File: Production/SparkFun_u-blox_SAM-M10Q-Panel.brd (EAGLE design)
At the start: 184.2 x 137.2 mm, 906 parts, among them J1 Qwiic Right Angle, J10 Qwiic Right Angle, J11 BOOT, J13 Qwiic Right Angle, J14 Qwiic Right Angle, J15 BOOT, J17 Qwiic Right Angle, J18 Qwiic Right Angle, J19 BOOT, J2 Qwiic Right Angle, J21 Qwiic Right Angle, J22 Qwiic Right Angle, J23 BOOT, J25 Qwiic Right Angle, J26 Qwiic Right Angle, J27 BOOT, J29 Qwiic Right Angle, J30 Qwiic Right Angle, J31 BOOT, J33 Qwiic Right Angle, J34 Qwiic Right Angle, J35 BOOT, J37 Qwiic Right Angle, J38 Qwiic Right Angle, J39 BOOT, J4 BOOT, J41 Qwiic Right Angle, J42 Qwiic Right Angle, J43 BOOT, J45 Qwiic Right Angle, J46 Qwiic Right Angle, J47 BOOT, J5 Qwiic Right Angle, J6 Qwiic Right Angle, J7 BOOT, J9 Qwiic Right Angle, U1 U-BLOX_SAM_M10Q-00B, U10 U-BLOX_SAM_M10Q-00B, U11 U-BLOX_SAM_M10Q-00B, U12 U-BLOX_SAM_M10Q-00B, U2 U-BLOX_SAM_M10Q-00B, U3 U-BLOX_SAM_M10Q-00B, U4 U-BLOX_SAM_M10Q-00B, U5 U-BLOX_SAM_M10Q-00B, U6 U-BLOX_SAM_M10Q-00B, U7 U-BLOX_SAM_M10Q-00B, U8 U-BLOX_SAM_M10Q-00B, U9 U-BLOX_SAM_M10Q-00B

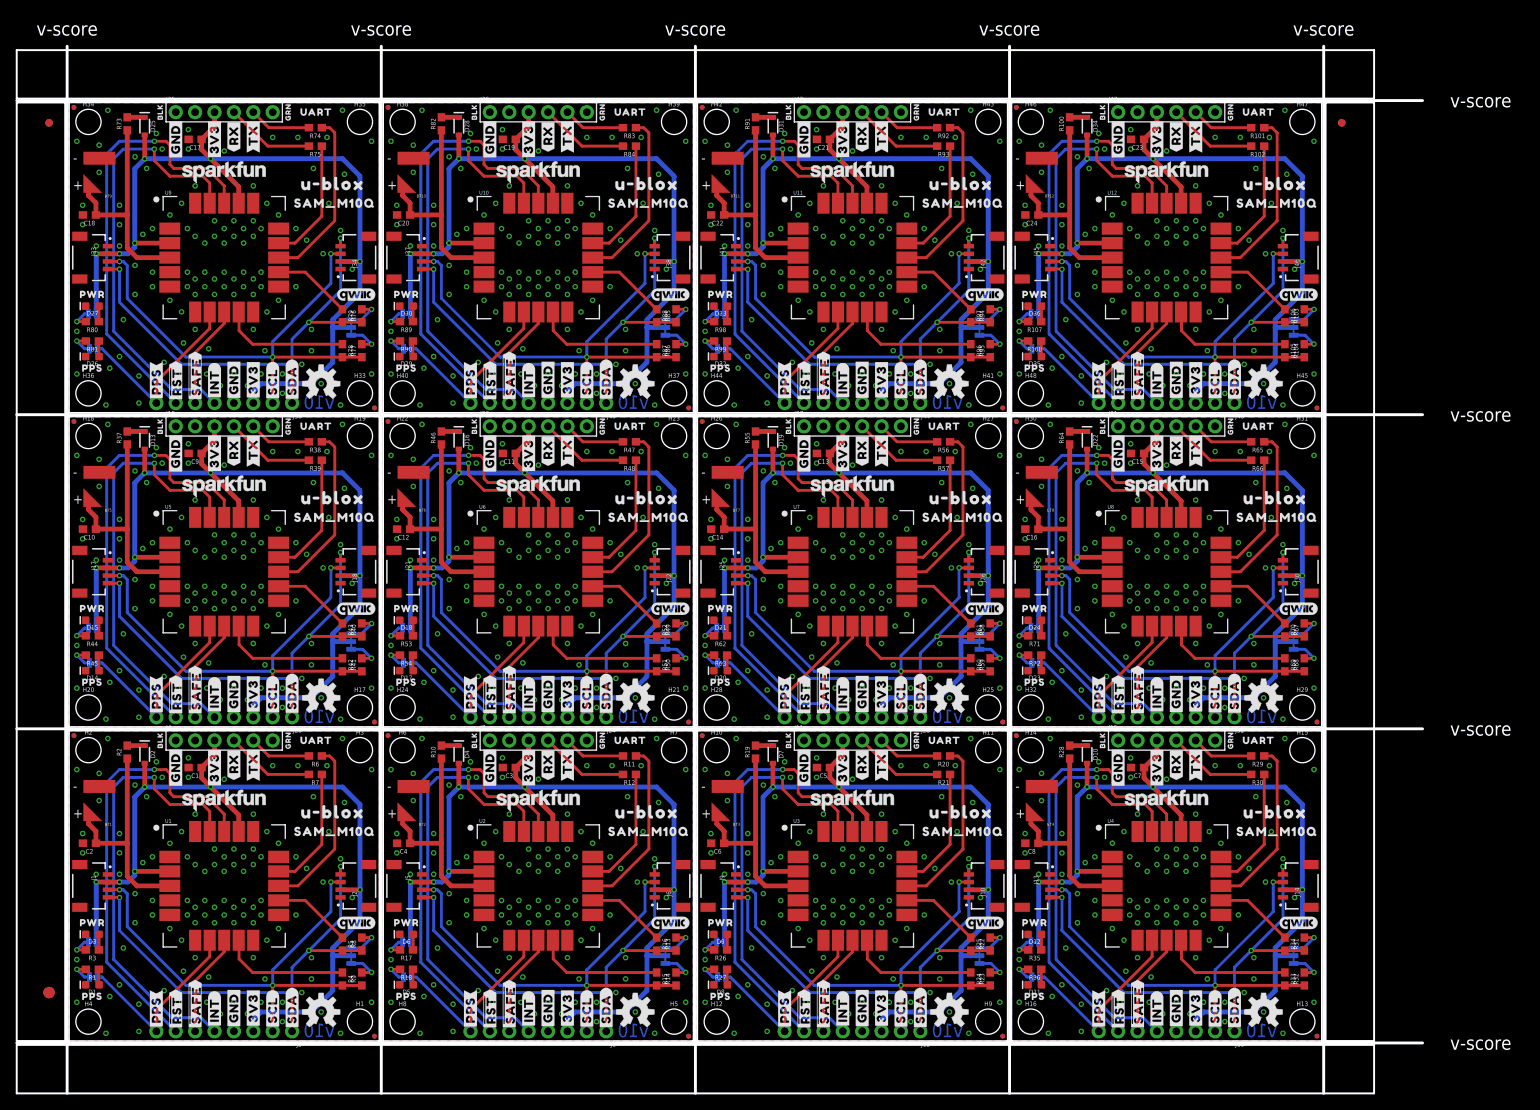
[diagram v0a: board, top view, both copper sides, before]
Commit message: Update post design review.
Swap for updated reflowable battery.
Adjust note for battery accordingly.
Add qwiic symbol in schematic, replacing silk only on board.
Expand t/b keepout under M10Q.
Swap SCL/SDA silk so they are on the correct pins.
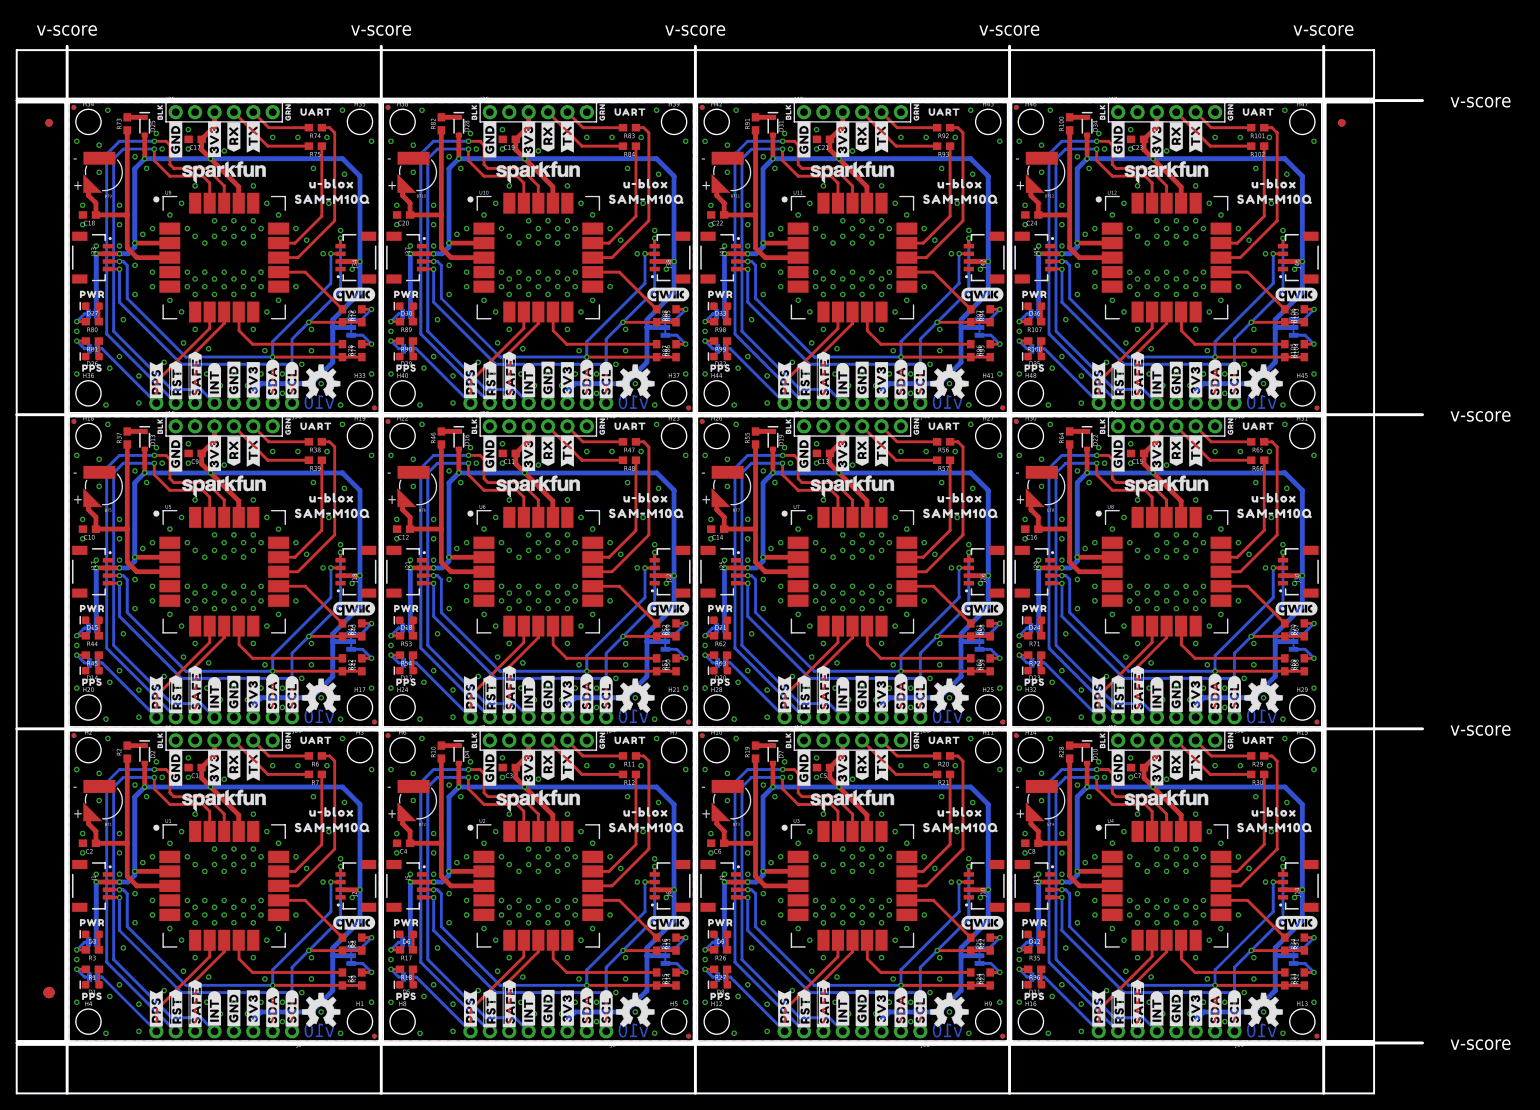
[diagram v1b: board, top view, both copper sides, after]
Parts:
- removed U$493, U$494: (no value), output:##RST##15
- removed U$495, U$496: (no value), output:##SAFE##16
- removed U$497: (no value), SparkFun-Aesthetics:SFE_LOGO_NAME_.1
- removed U$498, U$500: (no value), output:U#BLOX19
- removed U$499, U$501: (no value), output:SAM_M10Q0
- removed U$502: (no value), output:#PWRLED#0
- removed U$503: (no value), output:#PPSLED#0
- removed U$504: (no value), output:#I2CPUR#0
- added LOGO25, LOGO28, LOGO31, LOGO34: OSHW-LOGOM, SparkFun-Aesthetics:OSHW-LOGO-M
- added LOGO26, LOGO29, LOGO32, LOGO35: SFE_LOGO_NAME_FLAME.2_INCH, SparkFun-Aesthetics:SFE_LOGO_NAME_FLAME_.2
- added LOGO27, LOGO30, LOGO33, LOGO36: QWIIC_LOGO_CONNECTOR, SparkFun-Aesthetics:QWIIC_5.5MM
- BT1, BT10, BT11, BT12, BT2, BT3, BT4, BT5, BT6, BT7, BT8, BT9: device SparkFun-Batteries:ML414H_IV01E -> SparkFun-Batteries:MS421R_IV03E
- LOGO10, LOGO16, LOGO22, LOGO4: value SFE_LOGO_NAME_FLAME.2_INCH -> OSHW-LOGOM; device SparkFun-Aesthetics:SFE_LOGO_NAME_FLAME_.2 -> SparkFun-Aesthetics:OSHW-LOGO-M
- LOGO11, LOGO17, LOGO23, LOGO5: value OSHW-LOGOM -> SFE_LOGO_NAME_FLAME.2_INCH; device SparkFun-Aesthetics:OSHW-LOGO-M -> SparkFun-Aesthetics:SFE_LOGO_NAME_FLAME_.2
- LOGO12, LOGO18, LOGO24, LOGO6: value SFE_LOGO_NAME_FLAME.2_INCH -> QWIIC_LOGO_CONNECTOR; device SparkFun-Aesthetics:SFE_LOGO_NAME_FLAME_.2 -> SparkFun-Aesthetics:QWIIC_5.5MM
- LOGO15, LOGO21, LOGO3, LOGO9: value OSHW-LOGOM -> QWIIC_LOGO_CONNECTOR; device SparkFun-Aesthetics:OSHW-LOGO-M -> SparkFun-Aesthetics:QWIIC_5.5MM
- U$100, U$141, U$142, U$183: device output:#3V3#0 -> output:#GND#5
- U$101, U$59, U$60: device output:#GND#4 -> output:#GND#5
- U$102, U$143, U$144, U$185: device output:#GND#4 -> output:#3V3#0
- U$103, U$61, U$62: device output:#GND#5 -> output:#3V3#0
- U$104, U$145, U$146, U$187: device output:#GND#5 -> output:#SCL#6
- U$105, U$268, U$309, U$310, U$351, U$63, U$64: device output:#3V3#0 -> output:#SCL#6
- U$106, U$147, U$148, U$189, U$352, U$393, U$394, U$435: device output:#3V3#0 -> output:#SDA#7
- U$107, U$65, U$66: device output:#SCL#6 -> output:#SDA#7
- U$108, U$149, U$150, U$191: device output:#SCL#6 -> output:#INT#8
- U$109, U$67, U$68: device output:#SDA#7 -> output:#INT#8
- U$110, U$151, U$152, U$193: device output:#SDA#7 -> output:#PPS#13
- U$111, U$69, U$70: device output:#INT#8 -> output:#PPS#13
- U$112, U$153, U$154, U$195: device output:#INT#8 -> output:##RST##15
- U$113, U$71, U$72: device output:#PPS#13 -> output:##RST##15
- U$114, U$155, U$156, U$197: device output:#PPS#13 -> output:##SAFE##16
- U$115, U$73, U$74: device output:##RST##15 -> output:##SAFE##16
- U$116, U$157: device output:##RST##15 -> SparkFun-Aesthetics:SFE_LOGO_NAME_.1
- U$117, U$76: device output:##SAFE##16 -> output:#PWRLED#0
- U$118, U$159: device output:##SAFE##16 -> output:#PPSLED#0
- U$119: device SparkFun-Aesthetics:SFE_LOGO_NAME_.1 -> output:#I2CPUR#0
- U$120: device output:U#BLOX19 -> output:SAM#M10Q11
- U$121: device output:SAM_M10Q0 -> output:U#BLOX11
- U$122, U$204: device output:U#BLOX19 -> output:SAM#M10Q12
- U$123, U$205: device output:SAM_M10Q0 -> output:U#BLOX12
- U$124: device output:#PWRLED#0 -> SparkFun-Aesthetics:SFE_LOGO_FLAME_STOP_.1
- U$125, U$167: device output:#PPSLED#0 -> output:BLK4
- U$126, U$84: device output:#I2CPUR#0 -> output:BLK4
- U$127, U$169: device SparkFun-Aesthetics:SFE_LOGO_FLAME_STOP_.1 -> output:GRN5
- U$128, U$86: device SparkFun-Aesthetics:QWIIC_5MM -> output:GRN5
- U$129, U$130, U$171, U$88: device output:BLK4 -> output:UART7
- U$131, U$90: device output:GRN5 -> output:PPS9
- U$132, U$173: device output:GRN5 -> output:PWR10
- U$133, U$134, U$175, U$92: device output:UART7 -> output:#TX#12
- U$135, U$177: device output:PPS9 -> output:#RX#13
- U$136, U$94: device output:PWR10 -> output:#RX#13
- U$137, U$138, U$179, U$348, U$389, U$390, U$431, U$96: device output:#TX#12 -> output:#3V3#0
- U$139, U$140, U$181, U$98: device output:#RX#13 -> output:#GND#4
- U$158, U$199: device output:##RST##15 -> output:#PWRLED#0
- U$160, U$201: device output:##SAFE##16 -> output:#I2CPUR#0
- U$161: device SparkFun-Aesthetics:SFE_LOGO_NAME_.1 -> output:SAM#M10Q11
- U$162, U$18, U$80: device output:U#BLOX19 -> output:U#BLOX11
- U$163, U$32, U$81: device output:SAM_M10Q0 -> output:SAM#M10Q12
- U$164, U$246, U$38: device output:U#BLOX19 -> output:U#BLOX12
- U$165, U$247, U$39: device output:SAM_M10Q0 -> SparkFun-Aesthetics:SFE_LOGO_FLAME_STOP_.1
- U$166, U$208: device output:#PWRLED#0 -> output:BLK4
- U$168, U$210: device output:#I2CPUR#0 -> output:GRN5
- U$170, U$212: device SparkFun-Aesthetics:QWIIC_5MM -> output:UART7
- U$172, U$213: device output:BLK4 -> output:PPS9
- U$174, U$215, U$216, U$257: device output:GRN5 -> output:#TX#12
- U$176, U$217, U$218, U$259: device output:UART7 -> output:#RX#13
- U$178, U$220, U$430, U$472: device output:PWR10 -> output:#3V3#0
- U$180, U$221, U$222, U$263: device output:#TX#12 -> output:#GND#4
- U$182, U$223, U$224, U$265: device output:#RX#13 -> output:#GND#5
- U$186, U$227, U$228, U$269: device output:#GND#4 -> output:#SCL#6
- U$188, U$229, U$230, U$271: device output:#GND#5 -> output:#SDA#7
- U$190, U$231, U$232, U$273, U$436, U$477, U$478: device output:#3V3#0 -> output:#INT#8
- U$192, U$233, U$234, U$275: device output:#SCL#6 -> output:#PPS#13
- U$194, U$235, U$236, U$277: device output:#SDA#7 -> output:##RST##15
- U$196, U$237, U$238, U$279: device output:#INT#8 -> output:##SAFE##16
- U$198, U$239: device output:#PPS#13 -> SparkFun-Aesthetics:SFE_LOGO_NAME_.1
- U$2: device SparkFun-Aesthetics:QWIIC_5MM -> output:SAM#M10Q11
- U$200, U$241: device output:##RST##15 -> output:#PPSLED#0
- U$202, U$243: device output:##SAFE##16 -> output:SAM#M10Q11
- U$203: device SparkFun-Aesthetics:SFE_LOGO_NAME_.1 -> output:U#BLOX11
- U$206, U$288: device output:U#BLOX19 -> SparkFun-Aesthetics:SFE_LOGO_FLAME_STOP_.1
- U$207, U$249, U$289, U$331: device output:SAM_M10Q0 -> output:BLK4
- U$209, U$251: device output:#PPSLED#0 -> output:GRN5
- U$211, U$253: device SparkFun-Aesthetics:SFE_LOGO_FLAME_STOP_.1 -> output:UART7
- U$214, U$255: device output:BLK4 -> output:PWR10
- U$219, U$261, U$471: device output:PPS9 -> output:#3V3#0
- U$240, U$281: device output:#PPS#13 -> output:#PWRLED#0
- U$242, U$283: device output:##RST##15 -> output:#I2CPUR#0
- U$244, U$285: device output:##SAFE##16 -> output:U#BLOX11
- U$245: device SparkFun-Aesthetics:SFE_LOGO_NAME_.1 -> output:SAM#M10Q12
- U$248, U$290, U$330, U$372: device output:U#BLOX19 -> output:BLK4
- U$250, U$292: device output:#PWRLED#0 -> output:GRN5
- U$252, U$294: device output:#I2CPUR#0 -> output:UART7
- U$254: device SparkFun-Aesthetics:QWIIC_5MM -> output:PPS9
- U$256, U$297, U$298, U$339: device output:BLK4 -> output:#TX#12
- U$258, U$299, U$300, U$341: device output:GRN5 -> output:#RX#13
- U$260, U$301, U$302, U$343: device output:UART7 -> output:#3V3#0
- U$262, U$304: device output:PWR10 -> output:#GND#4
- U$264, U$305, U$306, U$347: device output:#TX#12 -> output:#GND#5
- U$266, U$307, U$308, U$349, U$55, U$56, U$97: device output:#RX#13 -> output:#3V3#0
- U$270, U$311, U$312, U$353: device output:#GND#4 -> output:#SDA#7
- U$272, U$313, U$314, U$355: device output:#GND#5 -> output:#INT#8
- U$274, U$315, U$316, U$357: device output:#3V3#0 -> output:#PPS#13
- U$276, U$317, U$318, U$359: device output:#SCL#6 -> output:##RST##15
- U$278, U$319, U$320, U$361: device output:#SDA#7 -> output:##SAFE##16
- U$280, U$321: device output:#INT#8 -> SparkFun-Aesthetics:SFE_LOGO_NAME_.1
- U$282, U$323: device output:#PPS#13 -> output:#PPSLED#0
- U$284, U$325: device output:##RST##15 -> output:SAM#M10Q11
- U$286, U$327: device output:##SAFE##16 -> output:SAM#M10Q12
- U$287: device SparkFun-Aesthetics:SFE_LOGO_NAME_.1 -> output:U#BLOX12
- U$291, U$333, U$373, U$415: device output:SAM_M10Q0 -> output:GRN5
- U$293, U$335: device output:#PPSLED#0 -> output:UART7
- U$295: device SparkFun-Aesthetics:SFE_LOGO_FLAME_STOP_.1 -> output:PPS9
- U$296: device SparkFun-Aesthetics:QWIIC_5MM -> output:PWR10
- U$303, U$345: device output:PPS9 -> output:#GND#4
- U$322, U$363: device output:#INT#8 -> output:#PWRLED#0
- U$324, U$365: device output:#PPS#13 -> output:#I2CPUR#0
- U$326, U$367: device output:##RST##15 -> output:U#BLOX11
- U$328, U$369: device output:##SAFE##16 -> output:U#BLOX12
- U$329: device SparkFun-Aesthetics:SFE_LOGO_NAME_.1 -> SparkFun-Aesthetics:SFE_LOGO_FLAME_STOP_.1
- U$332, U$374, U$414, U$456: device output:U#BLOX19 -> output:GRN5
- U$334, U$376: device output:#PWRLED#0 -> output:UART7
- U$336: device output:#I2CPUR#0 -> output:PPS9
- U$337: device SparkFun-Aesthetics:SFE_LOGO_FLAME_STOP_.1 -> output:PWR10
- U$338, U$380: device SparkFun-Aesthetics:QWIIC_5MM -> output:#TX#12
- U$340, U$381, U$382, U$423: device output:BLK4 -> output:#RX#13
- U$342, U$383, U$384, U$425: device output:GRN5 -> output:#3V3#0
- U$344, U$385, U$386, U$427: device output:UART7 -> output:#GND#4
- U$346, U$388: device output:PWR10 -> output:#GND#5
- U$350, U$391, U$392, U$433: device output:#RX#13 -> output:#SCL#6
- U$354, U$395, U$396, U$437: device output:#GND#4 -> output:#INT#8
- U$356, U$397, U$398, U$439: device output:#GND#5 -> output:#PPS#13
- U$358, U$399, U$400, U$441: device output:#3V3#0 -> output:##RST##15
- U$360, U$401, U$402, U$443: device output:#SCL#6 -> output:##SAFE##16
- U$362, U$403: device output:#SDA#7 -> SparkFun-Aesthetics:SFE_LOGO_NAME_.1
- U$364, U$405: device output:#INT#8 -> output:#PPSLED#0
- U$366, U$407: device output:#PPS#13 -> output:SAM#M10Q11
- U$368, U$409: device output:##RST##15 -> output:SAM#M10Q12
- U$370, U$411: device output:##SAFE##16 -> SparkFun-Aesthetics:SFE_LOGO_FLAME_STOP_.1
- U$371, U$413: device SparkFun-Aesthetics:SFE_LOGO_NAME_.1 -> output:BLK4
- U$375, U$417, U$457: device output:SAM_M10Q0 -> output:UART7
- U$377: device output:#PPSLED#0 -> output:PPS9
- U$378: device output:#I2CPUR#0 -> output:PWR10
- U$379, U$421: device SparkFun-Aesthetics:SFE_LOGO_FLAME_STOP_.1 -> output:#TX#12
- U$387, U$429: device output:PPS9 -> output:#GND#5
- U$404, U$445: device output:#SDA#7 -> output:#PWRLED#0
- U$406, U$447: device output:#INT#8 -> output:#I2CPUR#0
- U$408, U$449: device output:#PPS#13 -> output:U#BLOX11
- U$410, U$451: device output:##RST##15 -> output:U#BLOX12
- U$412, U$453, U$454: device output:##SAFE##16 -> output:BLK4
- U$416, U$458: device output:U#BLOX19 -> output:UART7
- U$418: device output:#PWRLED#0 -> output:PPS9
- U$419: device output:#PPSLED#0 -> output:PWR10
- U$420, U$462: device output:#I2CPUR#0 -> output:#TX#12
- U$422, U$464: device SparkFun-Aesthetics:QWIIC_5MM -> output:#RX#13
- U$424, U$465, U$466: device output:BLK4 -> output:#3V3#0
- U$426, U$467, U$468: device output:GRN5 -> output:#GND#4
- U$428, U$469, U$470: device output:UART7 -> output:#GND#5
- U$43, U$85: device SparkFun-Aesthetics:SFE_LOGO_FLAME_STOP_.1 -> output:BLK4
- U$432, U$473, U$474: device output:#TX#12 -> output:#SCL#6
- U$434, U$475, U$476: device output:#RX#13 -> output:#SDA#7
- U$438, U$479, U$480: device output:#GND#4 -> output:#PPS#13
- U$44: device SparkFun-Aesthetics:QWIIC_5MM -> output:BLK4
- U$440, U$481, U$482: device output:#GND#5 -> output:##RST##15
- U$442, U$483, U$484: device output:#3V3#0 -> output:##SAFE##16
- U$444, U$485: device output:#SCL#6 -> SparkFun-Aesthetics:SFE_LOGO_NAME_.1
- U$446, U$487: device output:#SDA#7 -> output:#PPSLED#0
- U$448, U$489: device output:#INT#8 -> output:SAM#M10Q11
- U$45, U$46, U$87: device output:BLK4 -> output:GRN5
- U$450, U$491: device output:#PPS#13 -> output:SAM#M10Q12
- U$452: device output:##RST##15 -> SparkFun-Aesthetics:SFE_LOGO_FLAME_STOP_.1
- U$455: device SparkFun-Aesthetics:SFE_LOGO_NAME_.1 -> output:GRN5
- U$459: device output:SAM_M10Q0 -> output:PPS9
- U$460: device output:#PWRLED#0 -> output:PWR10
- U$461: device output:#PPSLED#0 -> output:#TX#12
- U$463: device SparkFun-Aesthetics:SFE_LOGO_FLAME_STOP_.1 -> output:#RX#13
- U$47, U$48, U$89: device output:GRN5 -> output:UART7
- U$486: device output:#SCL#6 -> output:#PWRLED#0
- U$488: device output:#SDA#7 -> output:#I2CPUR#0
- U$49: device output:UART7 -> output:PPS9
- U$490: device output:#INT#8 -> output:U#BLOX11
- U$492: device output:#PPS#13 -> output:U#BLOX12
- U$50, U$91: device output:UART7 -> output:PWR10
- U$51, U$93: device output:PPS9 -> output:#TX#12
- U$52: device output:PWR10 -> output:#TX#12
- U$53, U$54, U$95: device output:#TX#12 -> output:#RX#13
- U$57, U$58, U$99: device output:#3V3#0 -> output:#GND#4
- U$75: device output:##SAFE##16 -> SparkFun-Aesthetics:SFE_LOGO_NAME_.1
- U$77: device SparkFun-Aesthetics:SFE_LOGO_NAME_.1 -> output:#PPSLED#0
- U$78: device output:U#BLOX19 -> output:#I2CPUR#0
- U$79: device output:SAM_M10Q0 -> output:SAM#M10Q11
- U$82: device output:#PWRLED#0 -> output:U#BLOX12
- U$83: device output:#PPSLED#0 -> SparkFun-Aesthetics:SFE_LOGO_FLAME_STOP_.1
- moved U$336 159.9 mm to (3.05, 88.1), flipped to the top, turned to 0 degrees
- moved U$331 155.6 mm to (11.9, 121.7), flipped to the bottom, turned to 90 degrees
- moved U$330 154.5 mm to (11.9, 121.7), turned to 90 degrees
- moved LOGO10 147.9 mm to (156.5, 3.81), flipped to the top
- moved U$168 147.5 mm to (28.7, 80.5), flipped to the top
- moved U$165 140.3 mm to (7.11, 43.7), flipped to the top
- moved U$167 138.5 mm to (11.9, 80.5), turned to 90 degrees
- moved U$329 137.2 mm to (7.11, 84.8)
- moved U$166 136.3 mm to (11.9, 80.5), flipped to the top, turned to 90 degrees
- moved U$333 134.1 mm to (28.7, 121.7), turned to 90 degrees
- moved U$332 132.8 mm to (28.7, 121.7), flipped to the top, turned to 90 degrees
- moved U$335 121.6 mm to (32.3, 121.7)
- moved LOGO15 119.7 mm to (37.3, 56.6)
- moved U$334 119.0 mm to (32.4, 121.7), flipped to the top
- moved LOGO12 109.4 mm to (160.8, 15.5), flipped to the top
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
